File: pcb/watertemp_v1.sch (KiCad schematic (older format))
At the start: 37 parts, among them J1 RN2483 Ext, J2 SWD, J3 I2C, J4 UART1, J5 UART0, Q1 Q_PMOS_GSD, Q2 Q_DUAL_NMOS_GSD_PMOS_SGD, U1 LPC11U24FBD48, U2 RN2483, U3 SHT21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

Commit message: Add TSOT26 footprint and regenerate netlist
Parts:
- Q2: footprint (none) -> TSOT_Custom:TSOT26
- R1, R2, R3, R6, R7, R8: footprint Resistors_SMD:R_0805_HandSoldering -> Resistors_SMD:R_0805
- R10, R11, R12, R9: footprint (none) -> Resistors_SMD:R_0805
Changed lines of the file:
@@
 F 0 "R1" V 9150 1450 50  0000 L CNN
 F 1 "470Ω" V 9350 1500 50  0000 L CNN
-F 2 "Resistors_SMD:R_0805_HandSoldering" H 9250 1500 50  0001 C CNN
+F 2 "Resistors_SMD:R_0805" H 9250 1500 50  0001 C CNN
 F 3 "" H 9250 1500 50  0001 C CNN
 	1    9250 1500
@@
 F 0 "R2" V 9600 1450 50  0000 L CNN
 F 1 "470Ω" V 9800 1500 50  0000 L CNN
-F 2 "Resistors_SMD:R_0805_HandSoldering" H 9700 1500 50  0001 C CNN
+F 2 "Resistors_SMD:R_0805" H 9700 1500 50  0001 C CNN
 F 3 "" H 9700 1500 50  0001 C CNN
 	1    9700 1500
@@
 F 0 "R3" V 10050 1450 50  0000 L CNN
 F 1 "470Ω" V 10250 1500 50  0000 L CNN
-F 2 "Resistors_SMD:R_0805_HandSoldering" H 10150 1500 50  0001 C CNN
+F 2 "Resistors_SMD:R_0805" H 10150 1500 50  0001 C CNN
 F 3 "" H 10150 1500 50  0001 C CNN
 	1    10150 1500
@@
 F 0 "R6" V 5450 5600 50  0000 L CNN
 F 1 "10KΩ" V 5650 5550 50  0000 L CNN
-F 2 "Resistors_SMD:R_0805_HandSoldering" H 5550 5650 50  0001 C CNN
+F 2 "Resistors_SMD:R_0805" H 5550 5650 50  0001 C CNN
 F 3 "" H 5550 5650 50  0001 C CNN
 	1    5550 5650
@@
 F 0 "R7" V 5450 5950 50  0000 L CNN
 F 1 "10KΩ" V 5650 5900 50  0000 L CNN
-F 2 "Resistors_SMD:R_0805_HandSoldering" H 5550 6000 50  0001 C CNN
+F 2 "Resistors_SMD:R_0805" H 5550 6000 50  0001 C CNN
 F 3 "" H 5550 6000 50  0001 C CNN
 	1    5550 6000
@@
 F 0 "R8" V 7650 4300 50  0000 L CNN
 F 1 "4.7K" H 7700 4350 50  0000 L CNN
-F 2 "Resistors_SMD:R_0805_HandSoldering" H 7650 4350 50  0001 C CNN
+F 2 "Resistors_SMD:R_0805" H 7650 4350 50  0001 C CNN
 F 3 "" H 7650 4350 50  0001 C CNN
 	1    7650 4350
@@
 F 0 "Q2" V 6250 2800 50  0000 L CNN
 F 1 "Q_DUAL_NMOS_GSD_PMOS_SGD" V 6350 2800 50  0000 L CNN
-F 2 "" H 6600 2800 50  0001 C CNN
+F 2 "TSOT_Custom:TSOT26" H 6600 2800 50  0001 C CNN
 F 3 "" H 6400 2650 50  0001 C CNN
 	2    6400 2650
@@
 F 0 "R11" H 5650 3250 50  0000 L CNN
 F 1 "10KΩ" H 5350 3250 50  0000 L CNN
-F 2 "" H 5600 3250 50  0001 C CNN
+F 2 "Resistors_SMD:R_0805" H 5600 3250 50  0001 C CNN
 F 3 "" H 5600 3250 50  0001 C CNN
 	1    5600 3250
@@
 F 0 "R12" H 6100 2750 50  0000 L CNN
 F 1 "10KΩ" H 6100 2650 50  0000 L CNN
-F 2 "" H 6000 2700 50  0001 C CNN
+F 2 "Resistors_SMD:R_0805" H 6000 2700 50  0001 C CNN
 F 3 "" H 6000 2700 50  0001 C CNN
 	1    6000 2700
@@
 F 0 "R9" H 7900 2800 50  0000 L CNN
 F 1 "6.04K 0.1%" H 7900 2700 50  0000 L CNN
-F 2 "" H 7800 2750 50  0001 C CNN
+F 2 "Resistors_SMD:R_0805" H 7800 2750 50  0001 C CNN
 F 3 "" H 7800 2750 50  0001 C CNN
 	1    7800 2750
@@
 F 0 "R10" H 7900 3200 50  0000 L CNN
 F 1 "9.30K 0.1%" H 7900 3100 50  0000 L CNN
-F 2 "" H 7800 3150 50  0001 C CNN
+F 2 "Resistors_SMD:R_0805" H 7800 3150 50  0001 C CNN
 F 3 "" H 7800 3150 50  0001 C CNN
 	1    7800 3150
@@
 F 0 "Q2" H 6100 3200 50  0000 L CNN
 F 1 "Q_DUAL_NMOS_GSD_PMOS_SGD" H 6100 3100 50  0000 L CNN
-F 2 "" H 6100 3250 50  0001 C CNN
+F 2 "TSOT_Custom:TSOT26" H 6100 3250 50  0001 C CNN
 F 3 "" H 5900 3100 50  0001 C CNN
 	1    5900 3100

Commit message: Add Digikey part number to RN248
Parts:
- U2: DigiKey (none) -> RN2483A-I/RM103-ND
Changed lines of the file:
@@
 F 2 "RN2483:RN2483" H 450 5100 60  0001 C CNN
 F 3 "" H 450 5100 60  0001 C CNN
+F 4 "RN2483A-I/RM103-ND" H 2250 6150 60  0001 C CNN "DigiKey"
 	1    2250 6150
 	1    0    0    -1

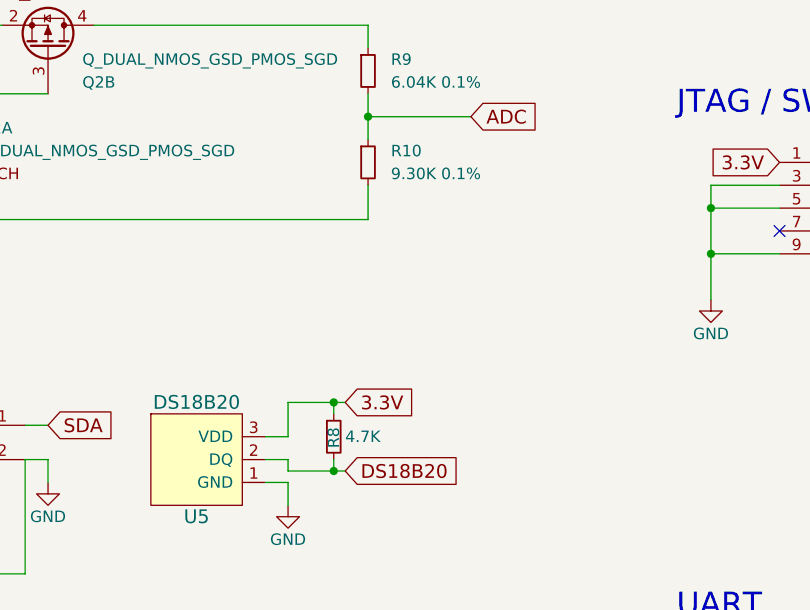
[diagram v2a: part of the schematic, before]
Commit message: Add order numbers to schema elements
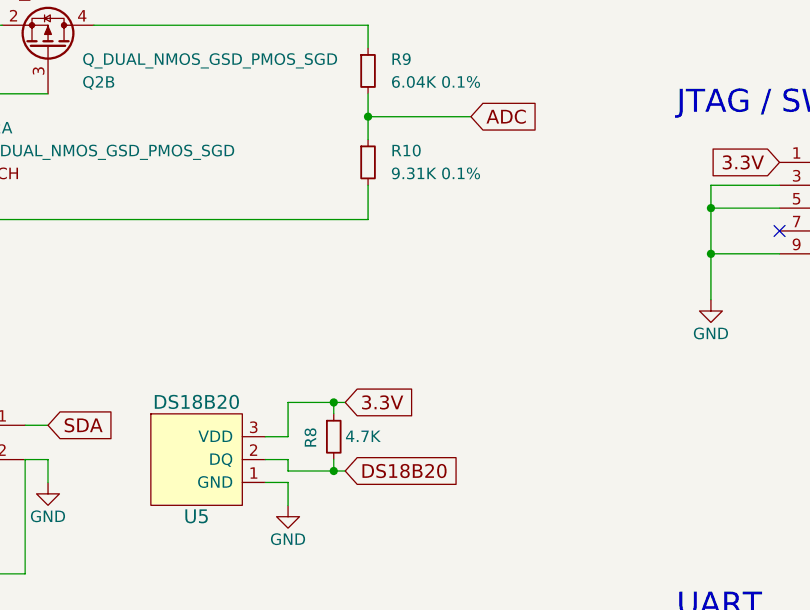
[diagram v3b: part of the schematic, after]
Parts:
- C5, C6, C7: Digikey (none) -> 1276-6468-1-ND
- D1: Digikey (none) -> 475-1278-1-ND
- D2: Digikey (none) -> 475-2560-1-ND
- D3: Digikey (none) -> 475-1410-1-ND
- Q2: Digikey (none) -> DMC2038LVT-7DICT-ND
- R1, R2, R3: Digikey (none) -> 311-470CRCT-ND
- R10: value 9.30K 0.1% -> 9.31K 0.1%; Digikey (none) -> YAG2002CT-ND
- R11, R12, R4, R5, R6, R7: Digikey (none) -> 311-10KARCT-ND
- R8: Digikey (none) -> 311-4.70KCRCT-ND
- R9: Digikey (none) -> P20683CT-ND
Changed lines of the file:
@@
 F 2 "Resistors_SMD:R_0805" V 730 5200 50  0001 C CNN
 F 3 "" H 800 5200 50  0001 C CNN
+F 4 "311-10KARCT-ND" V 800 5200 60  0001 C CNN "Digikey"
 	1    800  5200
 	1    0    0    -1
@@
 F 2 "Resistors_SMD:R_0805" H 9250 1500 50  0001 C CNN
 F 3 "" H 9250 1500 50  0001 C CNN
+F 4 "311-470CRCT-ND" V 9250 1500 60  0001 C CNN "Digikey"
 	1    9250 1500
 	1    0    0    -1
@@
 F 2 "Resistors_SMD:R_0805" H 9700 1500 50  0001 C CNN
 F 3 "" H 9700 1500 50  0001 C CNN
+F 4 "311-470CRCT-ND" V 9700 1500 60  0001 C CNN "Digikey"
 	1    9700 1500
 	1    0    0    -1
@@
 F 2 "Resistors_SMD:R_0805" H 10150 1500 50  0001 C CNN
 F 3 "" H 10150 1500 50  0001 C CNN
+F 4 "311-470CRCT-ND" V 10150 1500 60  0001 C CNN "Digikey"
 	1    10150 1500
 	1    0    0    -1
@@
 F 2 "LEDs:LED_0805" V 9250 1850 50  0001 C CNN
 F 3 "" V 9250 1850 50  0001 C CNN
+F 4 "475-1278-1-ND" H 9250 1850 60  0001 C CNN "Digikey"
 	1    9250 1850
 	0    -1   -1   0
@@
 F 2 "LEDs:LED_0805" V 9700 1850 50  0001 C CNN
 F 3 "" V 9700 1850 50  0001 C CNN
+F 4 "475-2560-1-ND" H 9700 1850 60  0001 C CNN "Digikey"
 	1    9700 1850
 	0    -1   -1   0
@@
 F 2 "LEDs:LED_0805" V 10150 1850 50  0001 C CNN
 F 3 "" V 10150 1850 50  0001 C CNN
+F 4 "475-1410-1-ND" H 10150 1850 60  0001 C CNN "Digikey"
 	1    10150 1850
 	0    -1   -1   0
@@
 F 2 "Resistors_SMD:R_0805" H 5550 5650 50  0001 C CNN
 F 3 "" H 5550 5650 50  0001 C CNN
+F 4 "311-10KARCT-ND" V 5550 5650 60  0001 C CNN "Digikey"
 	1    5550 5650
 	0    1    1    0
@@
 F 2 "Resistors_SMD:R_0805" H 5550 6000 50  0001 C CNN
 F 3 "" H 5550 6000 50  0001 C CNN
+F 4 "311-10KARCT-ND" V 5550 6000 60  0001 C CNN "Digikey"
 	1    5550 6000
 	0    1    1    0
@@
 F 2 "Resistors_SMD:R_0805" V 580 1000 50  0001 C CNN
 F 3 "" H 650 1000 50  0001 C CNN
+F 4 "311-10KARCT-ND" V 650 1000 60  0001 C CNN "Digikey"
 	1    650  1000
 	1    0    0    -1
@@
 U 1 1 59922965
 P 7650 4350
-F 0 "R8" V 7650 4300 50  0000 L CNN
+F 0 "R8" V 7550 4300 50  0000 L CNN
 F 1 "4.7K" H 7700 4350 50  0000 L CNN
 F 2 "Resistors_SMD:R_0805" H 7650 4350 50  0001 C CNN
 F 3 "" H 7650 4350 50  0001 C CNN
+F 4 "311-4.70KCRCT-ND" V 7650 4350 60  0001 C CNN "Digikey"
 	1    7650 4350
 	1    0    0    -1
@@
 F 2 "Capacitors_SMD:C_0805_HandSoldering" H 5800 4950 50  0001 C CNN
 F 3 "" H 5800 4950 50  0001 C CNN
+F 4 "1276-6468-1-ND" H 5800 4950 60  0001 C CNN "Digikey"
 	1    5800 4950
 	0    1    1    0
@@
 F 2 "Capacitors_SMD:C_0805" H 2750 900 50  0001 C CNN
 F 3 "" H 2750 900 50  0001 C CNN
+F 4 "1276-6468-1-ND" H 2750 900 60  0001 C CNN "Digikey"
 	1    2750 900
 	0    1    1    0
@@
 F 2 "Capacitors_SMD:C_0805" H 2150 900 50  0001 C CNN
 F 3 "" H 2150 900 50  0001 C CNN
+F 4 "1276-6468-1-ND" H 2150 900 60  0001 C CNN "Digikey"
 	1    2150 900
 	0    1    1    0
@@
 F 2 "TSOT_Custom:TSOT26" H 6600 2800 50  0001 C CNN
 F 3 "" H 6400 2650 50  0001 C CNN
+F 4 "DMC2038LVT-7DICT-ND" V 6400 2650 60  0001 C CNN "Digikey"
 	2    6400 2650
 	0    1    -1   0
@@
 F 2 "Resistors_SMD:R_0805" H 5600 3250 50  0001 C CNN
 F 3 "" H 5600 3250 50  0001 C CNN
+F 4 "311-10KARCT-ND" H 5600 3250 60  0001 C CNN "Digikey"
 	1    5600 3250
 	-1   0    0    1
@@
 F 2 "Resistors_SMD:R_0805" H 6000 2700 50  0001 C CNN
 F 3 "" H 6000 2700 50  0001 C CNN
+F 4 "311-10KARCT-ND" H 6000 2700 60  0001 C CNN "Digikey"
 	1    6000 2700
 	-1   0    0    1
@@
 F 2 "Resistors_SMD:R_0805" H 7800 2750 50  0001 C CNN
 F 3 "" H 7800 2750 50  0001 C CNN
+F 4 "P20683CT-ND" H 7800 2750 60  0001 C CNN "Digikey"
 	1    7800 2750
 	1    0    0    -1
@@
 P 7800 3150
 F 0 "R10" H 7900 3200 50  0000 L CNN
-F 1 "9.30K 0.1%" H 7900 3100 50  0000 L CNN
+F 1 "9.31K 0.1%" H 7900 3100 50  0000 L CNN
 F 2 "Resistors_SMD:R_0805" H 7800 3150 50  0001 C CNN
 F 3 "" H 7800 3150 50  0001 C CNN
+F 4 "YAG2002CT-ND" H 7800 3150 60  0001 C CNN "Digikey"
 	1    7800 3150
 	1    0    0    -1
@@
 F 2 "TSOT_Custom:TSOT26" H 6100 3250 50  0001 C CNN
 F 3 "" H 5900 3100 50  0001 C CNN
+F 4 "DMC2038LVT-7DICT-ND" H 5900 3100 60  0001 C CNN "Digikey"
 	1    5900 3100
 	1    0    0    -1
